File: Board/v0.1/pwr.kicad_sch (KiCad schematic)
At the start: 11 parts, among them U2 MAX1821

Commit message: Clean schematics (add date and revision...)
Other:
- company: (none) -> Bzgec
- title: (none) -> Power supply
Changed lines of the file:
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@@
 (kicad_sch (version 20211123) (generator eeschema)
   (paper "A4")
+  (title_block
+    (title "Power supply")
+    (date "2022/01/06")
+    (rev "v0.1")
+    (company "Bzgec")
+  )
   (junction (at 69.85 80.01) (diameter 0) (color 0 0 0 0)
   )
@@
   (symbol (lib_id "power:GND") (at 99.06 115.57 0) (unit 1)
     (in_bom yes) (on_board yes)
-    (property "Reference" "#PWR028" (id 0) (at 99.06 121.92 0)
+    (property "Reference" "#PWR027" (id 0) (at 99.06 121.92 0)
       (effects (font (size 1.27 1.27)) hide)
     )
@@
   (symbol (lib_id "power:GND") (at 105.41 115.57 0) (unit 1)
     (in_bom yes) (on_board yes)
-    (property "Reference" "#PWR029" (id 0) (at 105.41 121.92 0)
+    (property "Reference" "#PWR028" (id 0) (at 105.41 121.92 0)
       (effects (font (size 1.27 1.27)) hide)
     )
@@
   (symbol (lib_id "power:GND") (at 77.47 116.84 0) (unit 1)
     (in_bom yes) (on_board yes)
-    (property "Reference" "#PWR026" (id 0) (at 77.47 123.19 0)
+    (property "Reference" "#PWR025" (id 0) (at 77.47 123.19 0)
       (effects (font (size 1.27 1.27)) hide)
     )
@@
   (symbol (lib_id "power:GND") (at 124.46 123.19 0) (unit 1)
     (in_bom yes) (on_board yes)
-    (property "Reference" "#PWR030" (id 0) (at 124.46 129.54 0)
+    (property "Reference" "#PWR029" (id 0) (at 124.46 129.54 0)
       (effects (font (size 1.27 1.27)) hide)
     )
@@
   (symbol (lib_id "power:GND") (at 152.4 104.14 0) (unit 1)
     (in_bom yes) (on_board yes)
-    (property "Reference" "#PWR032" (id 0) (at 152.4 110.49 0)
+    (property "Reference" "#PWR031" (id 0) (at 152.4 110.49 0)
       (effects (font (size 1.27 1.27)) hide)
     )
@@
   (symbol (lib_id "power:GND") (at 86.36 96.52 0) (unit 1)
     (in_bom yes) (on_board yes)
-    (property "Reference" "#PWR027" (id 0) (at 86.36 102.87 0)
+    (property "Reference" "#PWR026" (id 0) (at 86.36 102.87 0)
       (effects (font (size 1.27 1.27)) hide)
     )
@@
   (symbol (lib_id "power:GNDPWR") (at 69.85 88.9 0) (unit 1)
     (in_bom yes) (on_board yes) (fields_autoplaced)
-    (property "Reference" "#PWR025" (id 0) (at 69.85 93.98 0)
+    (property "Reference" "#PWR024" (id 0) (at 69.85 93.98 0)
       (effects (font (size 1.27 1.27)) hide)
     )
@@
   (symbol (lib_id "power:GNDPWR") (at 49.53 180.34 0) (unit 1)
     (in_bom yes) (on_board yes) (fields_autoplaced)
-    (property "Reference" "#PWR023" (id 0) (at 49.53 185.42 0)
+    (property "Reference" "#PWR022" (id 0) (at 49.53 185.42 0)
       (effects (font (size 1.27 1.27)) hide)
     )
@@
   (symbol (lib_id "power:GND") (at 58.42 180.34 0) (unit 1)
     (in_bom yes) (on_board yes) (fields_autoplaced)
-    (property "Reference" "#PWR024" (id 0) (at 58.42 186.69 0)
+    (property "Reference" "#PWR023" (id 0) (at 58.42 186.69 0)
       (effects (font (size 1.27 1.27)) hide)
     )
@@
   (symbol (lib_id "power:GNDPWR") (at 130.81 87.63 0) (unit 1)
     (in_bom yes) (on_board yes) (fields_autoplaced)
-    (property "Reference" "#PWR031" (id 0) (at 130.81 92.71 0)
-      (effects (font (size 1.27 1.27)) hide)
-    )
+    (property "Reference" "#PWR030" (id 0) (at 130.81 92.71 0)
+      (effects (font (size 1.27 1.27)) hide)
+    )

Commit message: Add polyfuse, 3.3V status LED, USB_CONN sheet
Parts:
- added D2: ESD5Z3.3T1G, Diode_SMD:D_SOD-523, symbol Device:D_Zener
- added D3: GREEN_LED, Diode_SMD:D_0603_1608Metric_Pad1.05x0.95mm_HandSolder, symbol Device:LED
- added R20: 1.5k, Resistor_SMD:R_0603_1608Metric_Pad0.98x0.95mm_HandSolder, symbol Device:R
- renumbered C12 to C10, C13 to C11, C8 to C6, C9 to C7, C10 to C8, C11 to C9, R18 to R17, R19 to R18, R20 to R19
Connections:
- net GND: now also D2.2 (A), R20.2
- net Vin renamed +5V
- net Vout renamed +3V3
- net +3V3: now also D2.1 (K), D3.2 (A)
- new net: D3.1 (K), R20.1

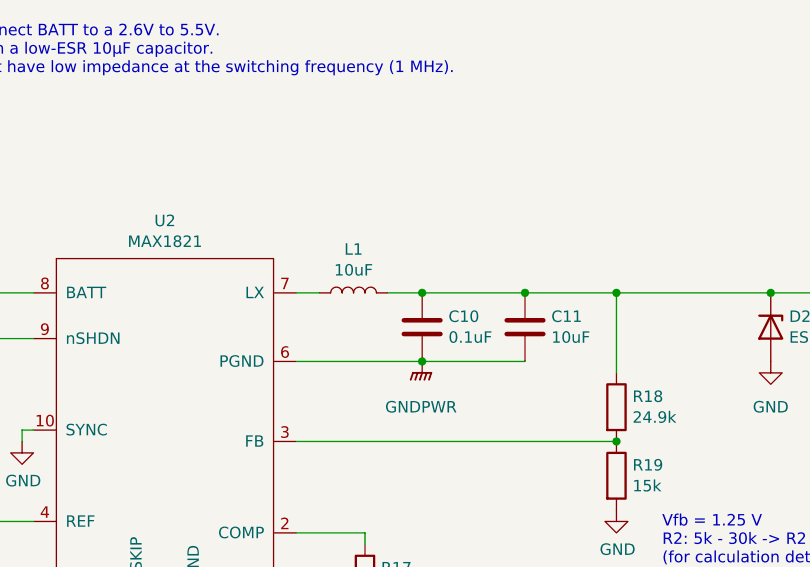
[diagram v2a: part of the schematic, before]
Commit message: Fix missing pad for H1, fix missing power input ERC error
ERC error was: Input power pin not driven by any output power pins.
Fix was adding PWR_FLAG power symbol after polyfuse or inductor.
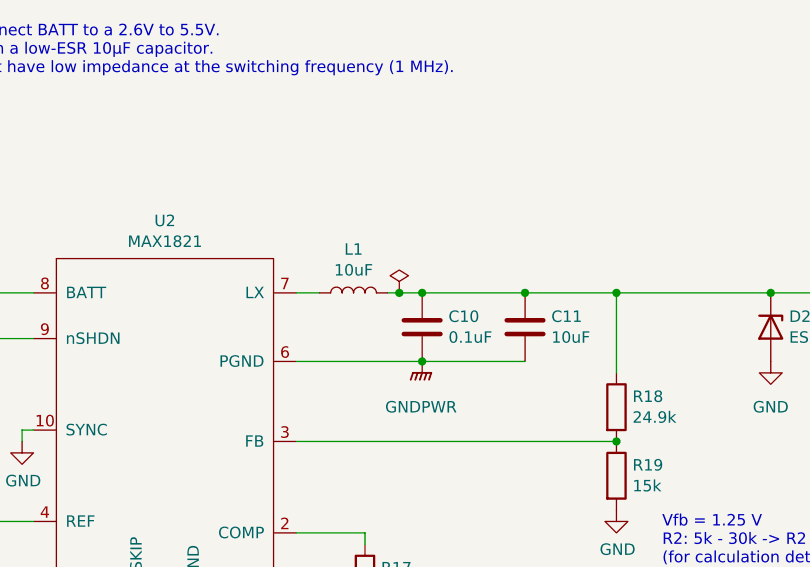
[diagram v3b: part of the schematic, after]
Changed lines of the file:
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@@
   (junction (at 169.545 80.01) (diameter 0) (color 0 0 0 0)
   )
+  (junction (at 128.27 80.01) (diameter 0) (color 0 0 0 0)
+  )
   (junction (at 81.28 80.01) (diameter 0) (color 0 0 0 0)
   )
@@
     (stroke (width 0) (type default) (color 0 0 0 0))
   )
+  (wire (pts (xy 128.27 80.01) (xy 130.81 80.01))
+    (stroke (width 0) (type default) (color 0 0 0 0))
+  )
   (wire (pts (xy 130.81 80.01) (xy 142.24 80.01))
     (stroke (width 0) (type default) (color 0 0 0 0))
@@
     (stroke (width 0) (type default) (color 0 0 0 0))
   )
-  (wire (pts (xy 127 80.01) (xy 130.81 80.01))
+  (wire (pts (xy 127 80.01) (xy 128.27 80.01))
     (stroke (width 0) (type default) (color 0 0 0 0))
   )
@@
     (pin "2")
   )
+  (symbol (lib_id "power:PWR_FLAG") (at 128.27 80.01 0) (unit 1)
+    (in_bom yes) (on_board yes) (fields_autoplaced)
+    (property "Reference" "#FLG0101" (id 0) (at 128.27 78.105 0)
+      (effects (font (size 1.27 1.27)) hide)
+    )
+    (property "Value" "PWR_FLAG" (id 1) (at 128.27 74.93 0)
+      (effects (font (size 1.27 1.27)) hide)
+    )
+    (property "Footprint" "" (id 2) (at 128.27 80.01 0)
+      (effects (font (size 1.27 1.27)) hide)
+    )
+    (property "Datasheet" "~" (id 3) (at 128.27 80.01 0)
+      (effects (font (size 1.27 1.27)) hide)
+    )
+    (pin "1")
+  )
   (symbol (lib_id "power:+5V") (at 55.88 80.01 0) (unit 1)

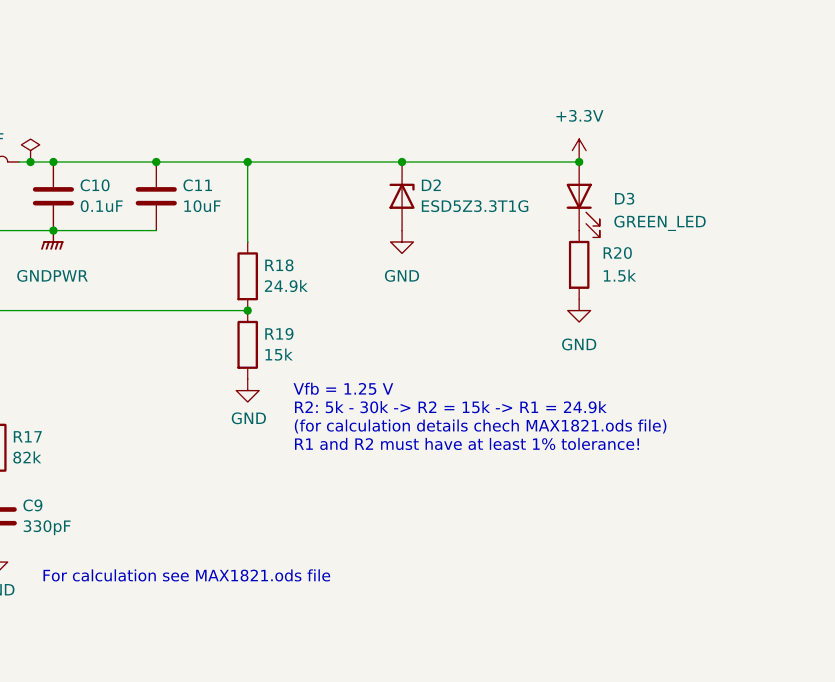
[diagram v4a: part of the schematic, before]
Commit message: Add jumper for 3.3V power LED
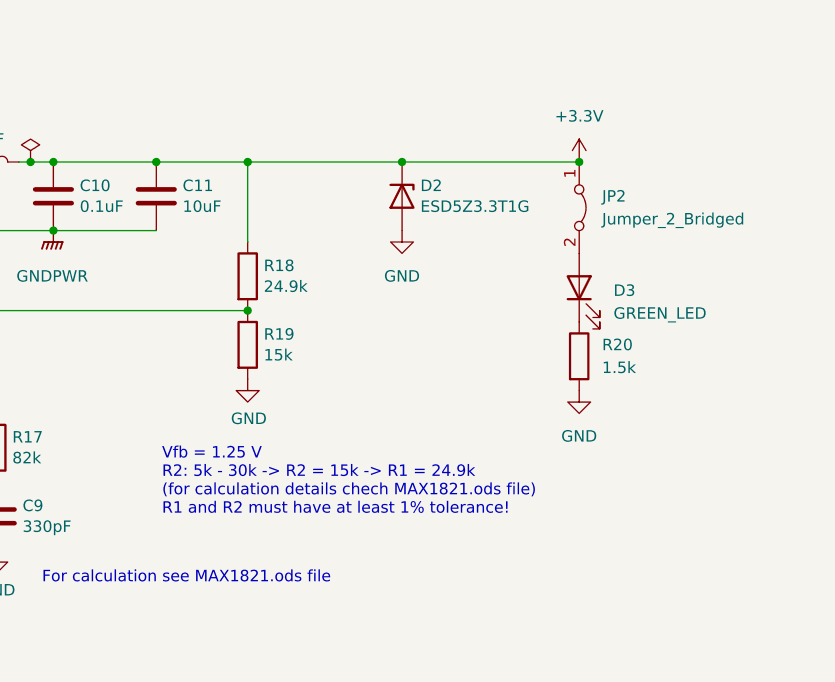
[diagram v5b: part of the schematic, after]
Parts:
- added JP2: Jumper_2_Bridged, Connector_PinHeader_2.54mm:PinHeader_1x02_P2.54mm_Horizontal, symbol Jumper:Jumper_2_Bridged
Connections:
- net +3V3: now also JP2.1 (A); no longer D3.2 (A)
- new net: D3.2 (A), JP2.2 (B)
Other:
- moved on the sheet: D3, R20
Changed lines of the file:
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@@
   (junction (at 169.545 80.01) (diameter 0) (color 0 0 0 0)
   )
+  (junction (at 189.23 80.01) (diameter 0) (color 0 0 0 0)
+  )
   (junction (at 128.27 80.01) (diameter 0) (color 0 0 0 0)
   )
   (junction (at 81.28 80.01) (diameter 0) (color 0 0 0 0)
   )
-  (junction (at 189.23 80.01) (diameter 0) (color 0 0 0 0)
-  )
   (junction (at 130.81 80.01) (diameter 0) (color 0 0 0 0)
   )
@@
   )
   (text "Vfb = 1.25 V\nR2: 5k - 30k -> R2 = 15k -> R1 = 24.9k\n(for calculation details chech MAX1821.ods file)\nR1 and R2 must have at least 1% tolerance!"
-    (at 157.48 112.395 0)
+    (at 142.875 119.38 0)
     (effects (font (size 1.27 1.27)) (justify left bottom))
   )
@@
     (pin "1")
   )
-  (symbol (lib_id "Device:LED") (at 189.23 83.82 90) (unit 1)
-    (in_bom yes) (on_board yes) (fields_autoplaced)
-    (property "Reference" "D3" (id 0) (at 193.04 84.1374 90)
+  (symbol (lib_id "Jumper:Jumper_2_Bridged") (at 189.23 85.09 270) (unit 1)
+    (in_bom yes) (on_board yes) (fields_autoplaced)
+    (property "Reference" "JP2" (id 0) (at 191.77 83.8199 90)
+      (effects (font (size 1.27 1.27)) (justify left))
+    )
+    (property "Value" "Jumper_2_Bridged" (id 1) (at 191.77 86.3599 90)
+      (effects (font (size 1.27 1.27)) (justify left))
+    )
+    (property "Footprint" "Connector_PinHeader_2.54mm:PinHeader_1x02_P2.54mm_Horizontal" (id 2) (at 189.23 85.09 0)
+      (effects (font (size 1.27 1.27)) hide)
+    )
+    (property "Datasheet" "~" (id 3) (at 189.23 85.09 0)
+      (effects (font (size 1.27 1.27)) hide)
+    )
+    (pin "1")
+    (pin "2")
+  )
+  (symbol (lib_id "Device:LED") (at 189.23 93.98 90) (unit 1)
+    (in_bom yes) (on_board yes) (fields_autoplaced)
+    (property "Reference" "D3" (id 0) (at 193.04 94.2974 90)
       (effects (font (size 1.27 1.27)) (justify right))
     )
-    (property "Value" "GREEN_LED" (id 1) (at 193.04 86.6774 90)
+    (property "Value" "GREEN_LED" (id 1) (at 193.04 96.8374 90)
       (effects (font (size 1.27 1.27)) (justify right))
     )
-    (property "Footprint" "Diode_SMD:D_0603_1608Metric_Pad1.05x0.95mm_HandSolder" (id 2) (at 189.23 83.82 0)
-      (effects (font (size 1.27 1.27)) hide)
-    )
-    (property "Datasheet" "~" (id 3) (at 189.23 83.82 0)
+    (property "Footprint" "Diode_SMD:D_0603_1608Metric_Pad1.05x0.95mm_HandSolder" (id 2) (at 189.23 93.98 0)
+      (effects (font (size 1.27 1.27)) hide)
+    )
+    (property "Datasheet" "~" (id 3) (at 189.23 93.98 0)
       (effects (font (size 1.27 1.27)) hide)
     )
@@
     (pin "1")
   )
-  (symbol (lib_id "Device:R") (at 189.23 91.44 0) (unit 1)
-    (in_bom yes) (on_board yes) (fields_autoplaced)
-    (property "Reference" "R20" (id 0) (at 191.77 90.1699 0)
-      (effects (font (size 1.27 1.27)) (justify left))
-    )
-    (property "Value" "1.5k" (id 1) (at 191.77 92.7099 0)
-      (effects (font (size 1.27 1.27)) (justify left))
-    )
-    (property "Footprint" "Resistor_SMD:R_0603_1608Metric_Pad0.98x0.95mm_HandSolder" (id 2) (at 187.452 91.44 90)
-      (effects (font (size 1.27 1.27)) hide)
-    )
-    (property "Datasheet" "~" (id 3) (at 189.23 91.44 0)
+  (symbol (lib_id "Device:R") (at 189.23 101.6 0) (unit 1)
+    (in_bom yes) (on_board yes) (fields_autoplaced)
+    (property "Reference" "R20" (id 0) (at 191.77 100.3299 0)
+      (effects (font (size 1.27 1.27)) (justify left))
+    )
+    (property "Value" "1.5k" (id 1) (at 191.77 102.8699 0)
+      (effects (font (size 1.27 1.27)) (justify left))
+    )
+    (property "Footprint" "Resistor_SMD:R_0603_1608Metric_Pad0.98x0.95mm_HandSolder" (id 2) (at 187.452 101.6 90)
+      (effects (font (size 1.27 1.27)) hide)
+    )
+    (property "Datasheet" "~" (id 3) (at 189.23 101.6 0)
       (effects (font (size 1.27 1.27)) hide)
     )
@@
     (pin "1")
   )
-  (symbol (lib_id "power:GND") (at 189.23 95.25 0) (unit 1)
-    (in_bom yes) (on_board yes) (fields_autoplaced)
-    (property "Reference" "#PWR027" (id 0) (at 189.23 101.6 0)
-      (effects (font (size 1.27 1.27)) hide)
-    )
-    (property "Value" "GND" (id 1) (at 189.23 100.33 0))
-    (property "Footprint" "" (id 2) (at 189.23 95.25 0)
-      (effects (font (size 1.27 1.27)) hide)
-    )
-    (property "Datasheet" "" (id 3) (at 189.23 95.25 0)
-      (effects (font (size 1.27 1.27)) hide)
-    )
+  (symbol (lib_id "power:GND") (at 189.23 105.41 0) (unit 1)
+    (in_bom yes) (on_board yes) (fields_autoplaced)
+    (property "Reference" "#PWR027" (id 0) (at 189.23 111.76 0)
+      (effects (font (size 1.27 1.27)) hide)
+    )
+    (property "Value" "GND" (id 1) (at 189.23 110.49 0))
+    (property "Footprint" "" (id 2) (at 189.23 105.41 0)
+      (effects (font (size 1.27 1.27)) hide)
+    )
+    (property "Datasheet" "" (id 3) (at 189.23 105.41 0)
+      (effects (font (size 1.27 1.27)) hide)
+    )
